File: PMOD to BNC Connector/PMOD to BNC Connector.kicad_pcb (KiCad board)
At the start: 2 copper layers, 50 x 85 mm, 16 parts, among them J1 Conn_01x06, J2 Conn_01x06, U1 RH-5000, U10 RH-5000, U2 RH-5000, U3 RH-5000, U4 RH-5000, U5 HL-BNC-KHDA, U6 HL-BNC-KHDA, U7 HL-BNC-KHDA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

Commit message: V2 Complete
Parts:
- added H1: MountingHole, MountingHole:MountingHole_3.5mm, F.Cu at (110.0, 142.5)
- added H2: MountingHole, MountingHole:MountingHole_3.5mm, F.Cu at (141.0, 142.5)
- added U11: RH-5000, New_test_point:CONN1_1514-2_KEY, F.Cu at (147.0, 128.6)
- added U12: RH-5000, New_test_point:CONN1_1514-2_KEY, F.Cu at (147.0, 156.4)
- U1, U10, U2, U3, U4, U9: footprint Test_point:TEST-TH_BD2.54-P1.4_RED -> New_test_point:CONN1_1514-2_KEY
- moved U10 7.27 mm to (147.0, 174.0), turned to 180 degrees
- moved U4 6.18 mm to (147.0, 165.2)
- moved U9 6.00 mm to (147.0, 111.0)
- moved TP1 5.50 mm to (147.5, 105.5)
- moved TP2 5.50 mm to (147.5, 179.5)
- moved U1 4.91 mm to (147.0, 119.8)
- moved U2 1.27 mm to (147.0, 137.4)
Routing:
- net Net-(J2-Pin_3): track 60.6 -> 65.1 mm
- net Net-(J1-Pin_1): track 49.2 -> 51.3 mm
- net Net-(J1-Pin_3): track 42.1 -> 42.6 mm
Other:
- outline, holes or cut-outs redrawn

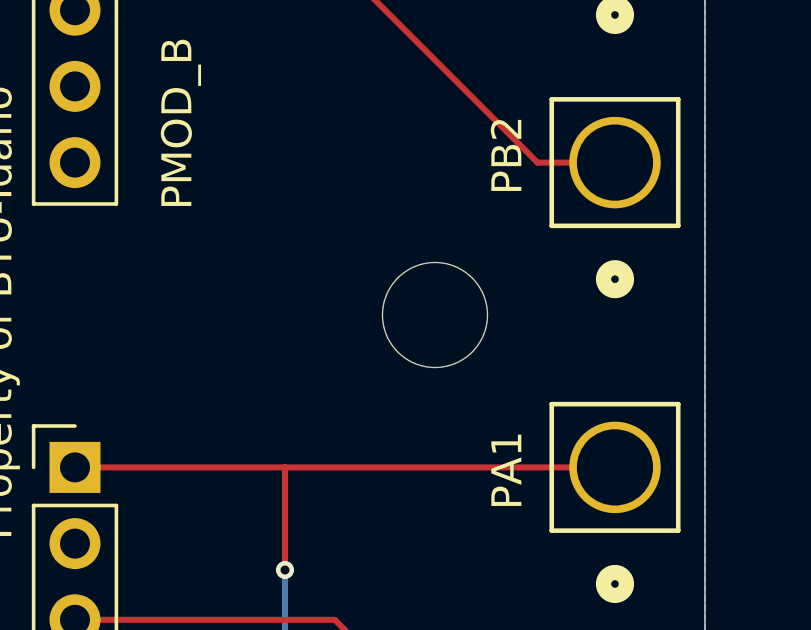
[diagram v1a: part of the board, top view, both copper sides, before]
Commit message: Version 2 Changes complete:
Thermal Relief for Ground-plane connected devices

Additional Mounting Holes Added

Additional Test Points to Ground Added

Cutout segment removed.
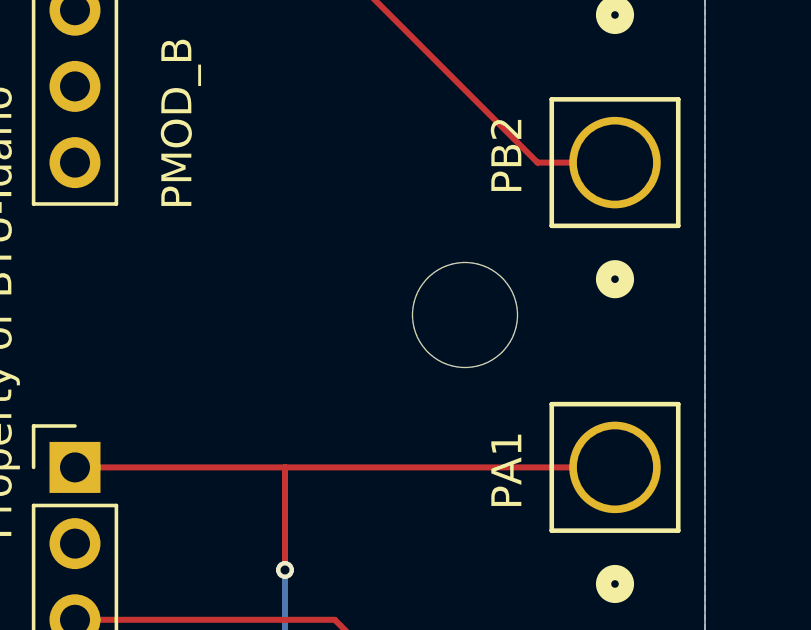
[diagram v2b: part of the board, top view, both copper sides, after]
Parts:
- moved H2 1.00 mm to (142.0, 142.5)
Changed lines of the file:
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@@
 	(footprint "MountingHole:MountingHole_3.5mm"
 		(layer "F.Cu")
-		(at 141 142.5)
+		(at 142 142.5)
 		(descr "Mounting Hole 3.5mm, no annular, generated by kicad-footprint-generator mountinghole.py")
 		(tags "mountinghole")
